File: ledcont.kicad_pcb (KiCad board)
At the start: 2 copper layers, 18.3 x 34 mm, 22 parts, among them J1 Screw_Terminal_01x02, J2 Screw_Terminal_01x02, U1 PAM2804, U2 TSM102A

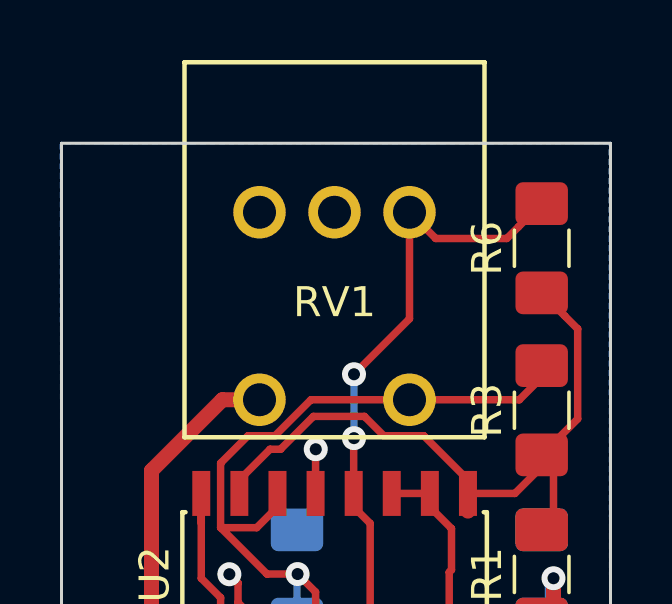
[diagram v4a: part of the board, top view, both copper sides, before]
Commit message: Reverse potentionmeter usage so that the LEDs start out dimmed.
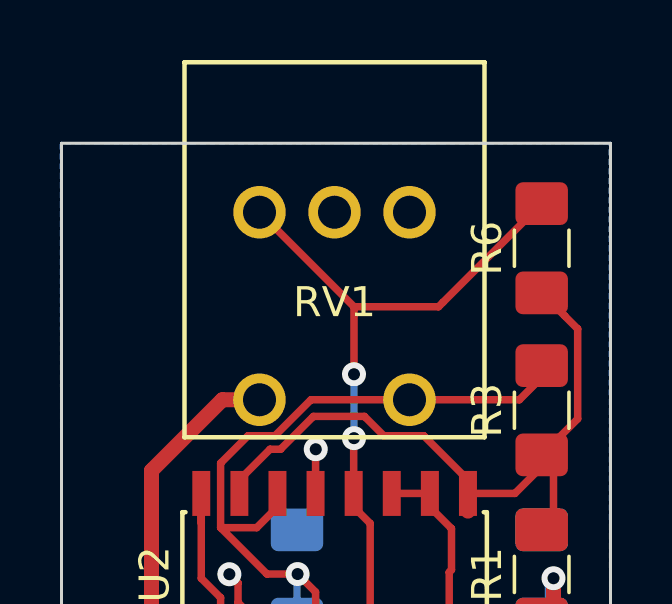
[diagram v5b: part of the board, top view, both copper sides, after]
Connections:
- RV1 pad 1: Net-(R6-Pad2) -> GND
- RV1 pad 3: GND -> Net-(R6-Pad2)
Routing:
- net Net-(R6-Pad2): track 21.2 -> 24.2 mm
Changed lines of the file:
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@@
     (thickness 1.6)
     (drawings 4)
-    (tracks 163)
+    (tracks 162)
     (zones 0)
     (modules 22)
@@
       (net 10 /Vswitch))
     (pad 3 thru_hole circle (at 2.5 10 180) (size 1.75 1.75) (drill 1.1) (layers *.Cu *.Mask)
-      (net 1 GND))
+      (net 7 "Net-(R6-Pad2)"))
     (pad 2 thru_hole circle (at 0 10 180) (size 1.75 1.75) (drill 1.1) (layers *.Cu *.Mask)
       (net 1 GND))
     (pad 1 thru_hole circle (at -2.5 10 180) (size 1.75 1.75) (drill 1.1) (layers *.Cu *.Mask)
-      (net 7 "Net-(R6-Pad2)"))
+      (net 1 GND))
   )
   (module ledcont:TSOT25 (layer F.Cu)
@@
   (gr_line (start 110.8 60.7) (end 110.8 94.7) (layer Edge.Cuts) (width 0.1))
   (gr_line (start 129.1 60.7) (end 110.8 60.7) (layer Edge.Cuts) (width 0.1))
-  (segment (start 116.729 77.379) (end 116.729 77.773) (width 0.25) (layer F.Cu) (net 10))
   (segment (start 119.269 72.373) (end 119.269 70.905994) (width 0.25) (layer F.Cu) (net 1))
   (segment (start 119.269 70.905994) (end 119.274994 70.9) (width 0.25) (layer F.Cu) (net 1))
@@
   (segment (start 121.543005 70.450001) (end 122.876001 70.450001) (width 0.25) (layer F.Cu) (net 6))
   (segment (start 118.101983 70.900012) (end 119.196997 69.804998) (width 0.25) (layer F.Cu) (net 6))
-  (segment (start 126.0348 63.483847) (end 126.806147 62.7125) (width 0.25) (layer F.Cu) (net 7))
-  (segment (start 125.643648 63.874999) (end 126.0348 63.483847) (width 0.25) (layer F.Cu) (net 7))
-  (segment (start 123.274999 63.874999) (end 125.643648 63.874999) (width 0.25) (layer F.Cu) (net 7))
-  (segment (start 122.4 63) (end 123.274999 63.874999) (width 0.25) (layer F.Cu) (net 7))
   (via (at 120.55 70.53) (size 0.8) (drill 0.4) (layers F.Cu B.Cu) (net 7))
   (segment (start 120.539 70.541) (end 120.55 70.53) (width 0.25) (layer F.Cu) (net 7))
@@
   (via (at 120.55 68.4) (size 0.8) (drill 0.4) (layers F.Cu B.Cu) (net 7))
   (segment (start 120.55 70.53) (end 120.55 68.4) (width 0.25) (layer B.Cu) (net 7))
-  (segment (start 122.4 66.55) (end 122.4 63) (width 0.25) (layer F.Cu) (net 7))
-  (segment (start 120.55 68.4) (end 122.4 66.55) (width 0.25) (layer F.Cu) (net 7))
   (segment (start 121.089 76.773) (end 120.539 77.323) (width 0.25) (layer F.Cu) (net 7))
   (segment (start 120.539 77.323) (end 120.539 77.773) (width 0.25) (layer F.Cu) (net 7))
@@
   (segment (start 120.539 72.373) (end 120.539 72.823) (width 0.25) (layer F.Cu) (net 7))
   (segment (start 121.089 73.373) (end 121.089 76.773) (width 0.25) (layer F.Cu) (net 7))
+  (segment (start 120.55 66.15) (end 120.55 68.4) (width 0.25) (layer F.Cu) (net 7))
+  (segment (start 117.4 63) (end 120.55 66.15) (width 0.25) (layer F.Cu) (net 7))
+  (segment (start 126.806147 62.7125) (end 123.518647 66) (width 0.25) (layer F.Cu) (net 7))
+  (segment (start 123.368647 66.15) (end 123.518647 66) (width 0.25) (layer F.Cu) (net 7))
+  (segment (start 120.55 66.15) (end 123.368647 66.15) (width 0.25) (layer F.Cu) (net 7))
   (segment (start 125.5615 76.5605) (end 124.349 77.773) (width 0.25) (layer F.Cu) (net 8))
   (segment (start 127.156147 76.5605) (end 125.5615 76.5605) (width 0.25) (layer F.Cu) (net 8))
@@
   (segment (start 123.800002 73.544002) (end 123.800002 74.923002) (width 0.25) (layer F.Cu) (net 9))
   (segment (start 125.916153 79.508653) (end 126.6875 80.28) (width 0.25) (layer F.Cu) (net 9))
+  (segment (start 116.729 77.379) (end 116.729 77.773) (width 0.25) (layer F.Cu) (net 10))
   (segment (start 118.4365 80.3) (end 118.4165 80.28) (width 0.25) (layer F.Cu) (net 10))
   (segment (start 119.269 77.773) (end 119.269 78.223) (width 0.25) (layer F.Cu) (net 10))

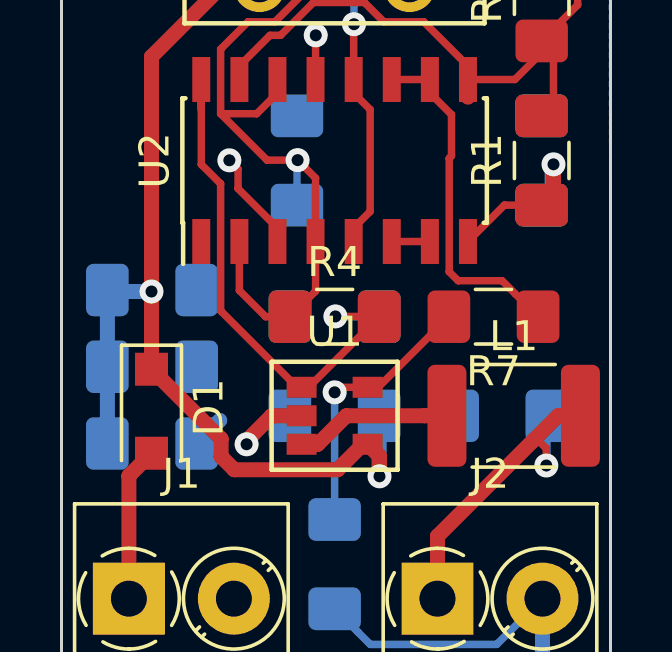
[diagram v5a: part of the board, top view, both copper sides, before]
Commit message: Switched PAM2804 to a standard TSOT-23-5 footprint.
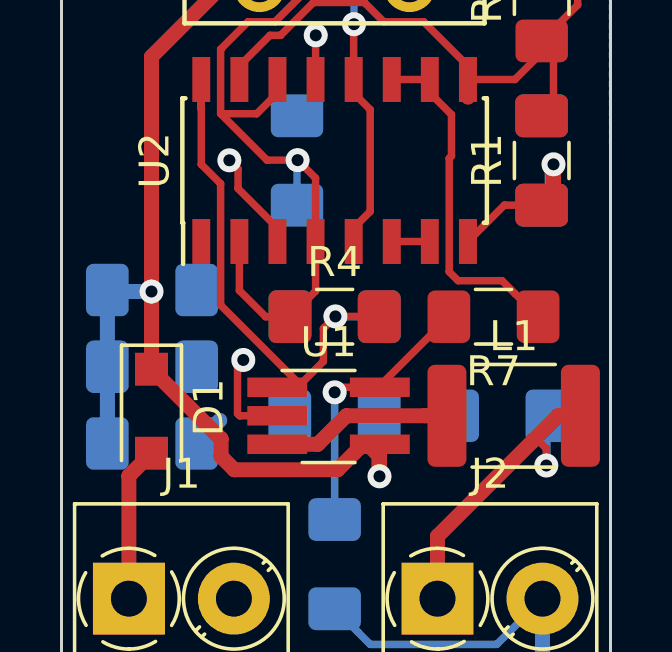
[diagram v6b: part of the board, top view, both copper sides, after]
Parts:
- U1: footprint ledcont:TSOT25 -> Package_TO_SOT_SMD:TSOT-23-5_HandSoldering
- moved U1 0.20 mm to (119.7, 83.6), turned to 0 degrees
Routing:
- net GND: track 8.33 -> 9.16 mm

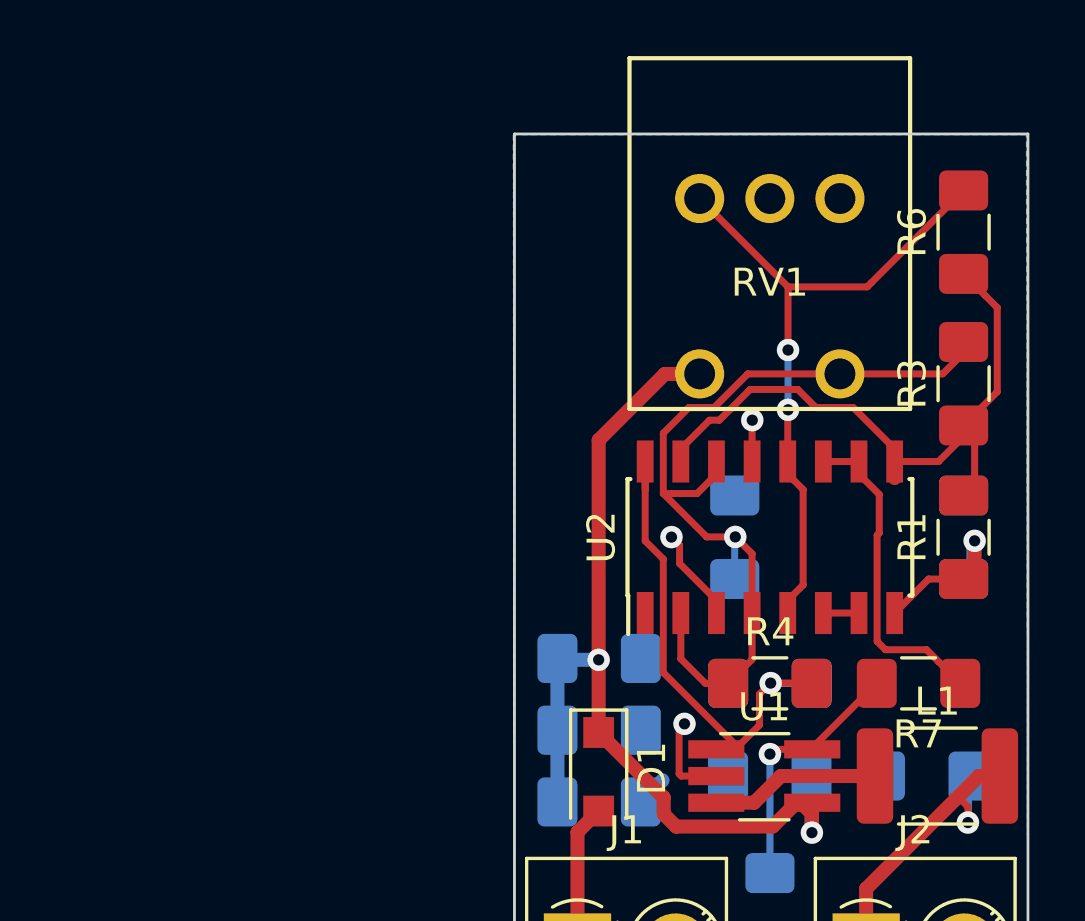
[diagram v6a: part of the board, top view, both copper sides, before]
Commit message: Start transitioning to lower-voltage parts.
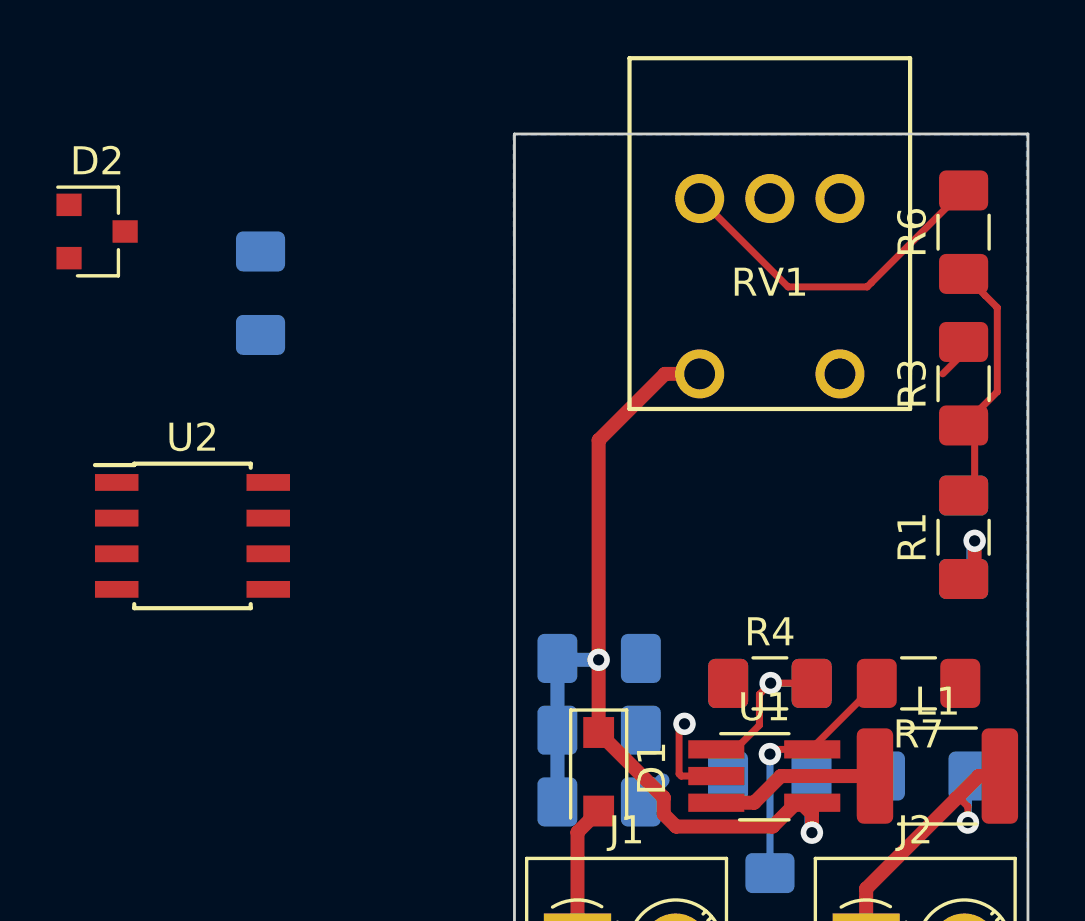
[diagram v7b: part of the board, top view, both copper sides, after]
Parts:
- added D2: TL431DBZ, Package_TO_SOT_SMD:SOT-23, F.Cu at (95.9, 64.2)
- R1: value 2k -> 0
- R2: value 10k -> NP
- R4: value 1k -> ?
- R6: value 20k -> ?
- R7: value 9k -> ?
- U2: value TSM102A -> MCP6002-xSN; footprint Package_SO:SOIC-16_3.9x9.9mm_P1.27mm -> Package_SO:SOIC-8_3.9x4.9mm_P1.27mm
- moved U2 20.6 mm to (99.3, 75.0), turned to 0 degrees
- moved C4 19.0 mm to (101.8, 66.4)
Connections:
- C4 pad 1: /Vswitch -> Net-(C4-Pad1)
- R1 pad 1: Net-(R1-Pad1) -> Net-(D2-Pad2)
- R2 pad 2: Net-(R1-Pad1) -> Net-(D2-Pad2)
- R3 pad 2: /Vswitch -> Net-(C4-Pad1)
- R4 pad 1: /Vswitch -> Net-(R4-Pad1)
- R4 pad 2: /Ven -> Net-(C4-Pad1)
- R7 pad 1: Net-(R7-Pad1) -> GND
- R7 pad 2: /Vfb -> Net-(R4-Pad1)
- RV1 pad 1: GND -> Net-(R6-Pad2)
- RV1 pad 2: GND -> Net-(RV1-Pad2)
- RV1 pad 3: Net-(R6-Pad2) -> GND
- RV1 pad 4: /Vswitch -> Net-(RV1-Pad4)
- U2 pad 1: Net-(U2-Pad1) -> /Ven
- U2 pad 2: /Vswitch -> Vref
- U2 pad 3: GND -> Net-(R4-Pad1)
- U2 pad 4: /Vswitch -> GND
- U2 pad 5: Net-(R6-Pad2) -> Net-(RV1-Pad2)
- U2 pad 8: Net-(R1-Pad1) -> Net-(C4-Pad1)
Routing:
- net /Vswitch: track 31.9 -> 0.00 mm, vias 1 -> 0
- net Vref: track 23.2 -> 9.39 mm
- net /Ven: track 19.8 -> 7.15 mm
- net Net-(R6-Pad2): track 24.2 -> 12.1 mm, vias 2 -> 0
- net Net-(R7-Pad1): track 11.6 -> 0.00 mm
- net Net-(R1-Pad1): track 6.07 -> 0.00 mm, vias 1 -> 0
- net GND: track 9.16 -> 4.31 mm, vias 3 -> 1
- net Net-(D2-Pad2): track 0.00 -> 2.76 mm, vias 0 -> 1
- net Net-(RV2-Pad2): track 1.72 -> 0.00 mm
- net Net-(C4-Pad1): track 0.00 -> 1.61 mm

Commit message: More board updates.
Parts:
- added R10: 10k, Resistor_SMD:R_0603_1608Metric_Pad1.05x0.95mm_HandSolder, F.Cu at (124.0, 79.9)
- added R11: 0, Resistor_SMD:R_0603_1608Metric_Pad1.05x0.95mm_HandSolder, F.Cu at (123.1, 77.2)
- added R12: 0, Resistor_SMD:R_0603_1608Metric_Pad1.05x0.95mm_HandSolder, F.Cu at (118.7, 80.0)
- added RV2: 5k, ledcont:TC33X, F.Cu at (126.7, 79.0)
- D2: value TL431DBZ -> TLV431
- R1, R2, R3: footprint Resistor_SMD:R_1206_3216Metric_Pad1.42x1.75mm_HandSolder -> Resistor_SMD:R_0603_1608Metric_Pad1.05x0.95mm_HandSolder
- R4: value ? -> 10k; footprint Resistor_SMD:R_1206_3216Metric_Pad1.42x1.75mm_HandSolder -> Resistor_SMD:R_0603_1608Metric_Pad1.05x0.95mm_HandSolder
- R5: footprint Resistor_SMD:R_1206_3216Metric_Pad1.42x1.75mm_HandSolder -> Resistor_SMD:R_0603_1608Metric_Pad1.05x0.95mm_HandSolder; moved to F.Cu
- R6: value ? -> 0; footprint Resistor_SMD:R_1206_3216Metric_Pad1.42x1.75mm_HandSolder -> Resistor_SMD:R_0603_1608Metric_Pad1.05x0.95mm_HandSolder
- R7: value ? -> 7k; footprint Resistor_SMD:R_1206_3216Metric_Pad1.42x1.75mm_HandSolder -> Resistor_SMD:R_0603_1608Metric_Pad1.05x0.95mm_HandSolder; moved to B.Cu
- moved D2 32.5 mm to (126.8, 74.2)
- moved C4 18.2 mm to (117.5, 75.6)
- moved U2 18.2 mm to (117.5, 75.6), turned to 180 degrees
- moved R4 7.53 mm to (122.7, 73.3), turned to 90 degrees
- moved R7 7.43 mm to (122.7, 73.3), turned to 270 degrees
- moved R1 3.47 mm to (126.8, 71.6), turned to 180 degrees
- moved R2 3.47 mm to (126.8, 71.6), turned to 0 degrees
- moved R6 2.50 mm to (126.7, 66.7), turned to 180 degrees
- moved R3 1.30 mm to (126.7, 68.3), turned to 180 degrees
- moved R5 0.41 mm to (120.2, 80.0), turned to 270 degrees
- moved RV1 0.27 mm to (119.6, 73.0)
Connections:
- C4 pad 1: Net-(C4-Pad1) -> /Vswitch
- R3 pad 2: Net-(C4-Pad1) -> /Vswitch
- R4 pad 2: Net-(C4-Pad1) -> /Vswitch
- RV1 pad 4: Net-(RV1-Pad4) -> /Vswitch
- U1 pad 1: /Ven -> Net-(R12-Pad1)
- U2 pad 8: Net-(C4-Pad1) -> /Vswitch
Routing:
- net /Vswitch: track 0.00 -> 28.1 mm, vias 0 -> 1
- net Net-(RV1-Pad2): track 0.00 -> 13.0 mm
- net Net-(R11-Pad2): track 0.00 -> 9.09 mm
- net Net-(R11-Pad1): track 0.00 -> 7.61 mm
- net Net-(R6-Pad2): track 12.1 -> 5.24 mm
- net Net-(R4-Pad1): track 0.03 -> 6.54 mm, vias 0 -> 1
- net GND: track 4.31 -> 10.1 mm, vias 1 -> 4
- net Vref: track 9.39 -> 14.1 mm
- net Net-(D2-Pad2): track 2.76 -> 7.16 mm
- net /Ven: track 7.15 -> 3.67 mm, vias 1 -> 0
- net /Vin: track 34.2 -> 37.0 mm
- net Net-(R12-Pad1): track 0.00 -> 2.73 mm
- net Net-(R10-Pad1): track 0.00 -> 2.60 mm
- net Net-(C4-Pad1): track 1.61 -> 0.00 mm
